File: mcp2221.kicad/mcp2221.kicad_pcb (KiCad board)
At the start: 2 copper layers, 71.5 x 45.4 mm, 24 parts, among them J1 Conn_01x07_Male, J2 Jumper 32 or 21, J3 Conn_01x02_Male, J4 Conn_01x02_Male, J5 Conn_01x04_Male, J6 Conn_01x03_Male, J7 Conn_01x03_Male, SW1 SW_Push, U1 AMS1117CD-3.3, U2 MCP2221

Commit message: pcb layout changes
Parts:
- moved SW1 36.7 mm to (111.8, 48.0), turned to 270 degrees
- moved R5 33.6 mm to (101.7, 49.1), turned to 270 degrees
- moved R8 32.0 mm to (74.0, 76.5), turned to 180 degrees
- moved J4 29.6 mm to (105.3, 49.9), turned to 0 degrees
- moved J3 23.9 mm to (87.2, 83.2)
- moved R1 22.3 mm to (106.8, 80.4), turned to 90 degrees
- moved R4 17.0 mm to (76.7, 82.7)
- moved J7 10.6 mm to (77.3, 77.3)
- moved J6 10.5 mm to (77.3, 73.5)
- moved R6 10.5 mm to (66.4, 73.7)
- moved R9 10.5 mm to (66.4, 82.7)
- moved D2 8.26 mm to (71.9, 79.8)
- moved D1 4.11 mm to (69.0, 79.6), turned to 180 degrees
- moved J1 1.68 mm to (91.4, 86.1)
- moved R7 1.61 mm to (74.0, 85.6), turned to 180 degrees
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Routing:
- added copper zone on B.Cu, net GND

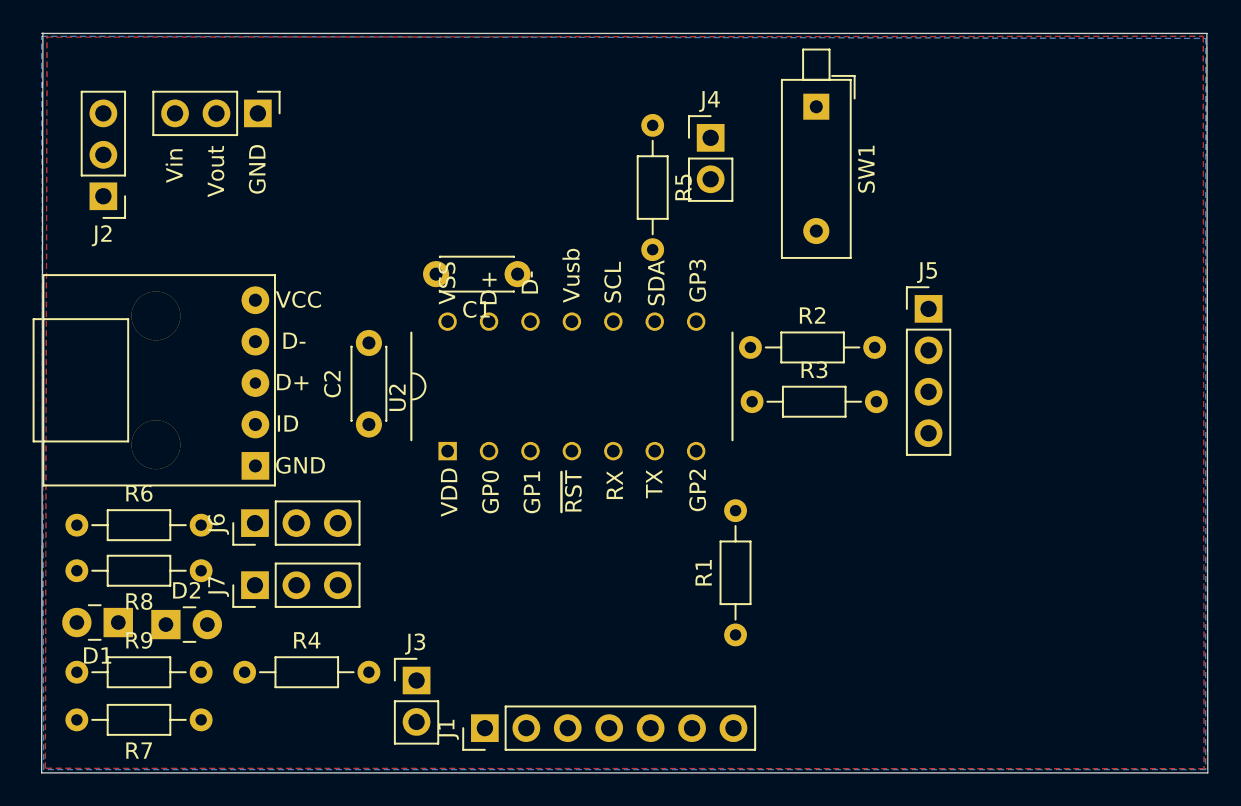
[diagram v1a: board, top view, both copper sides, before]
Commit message: initial layout for SMD
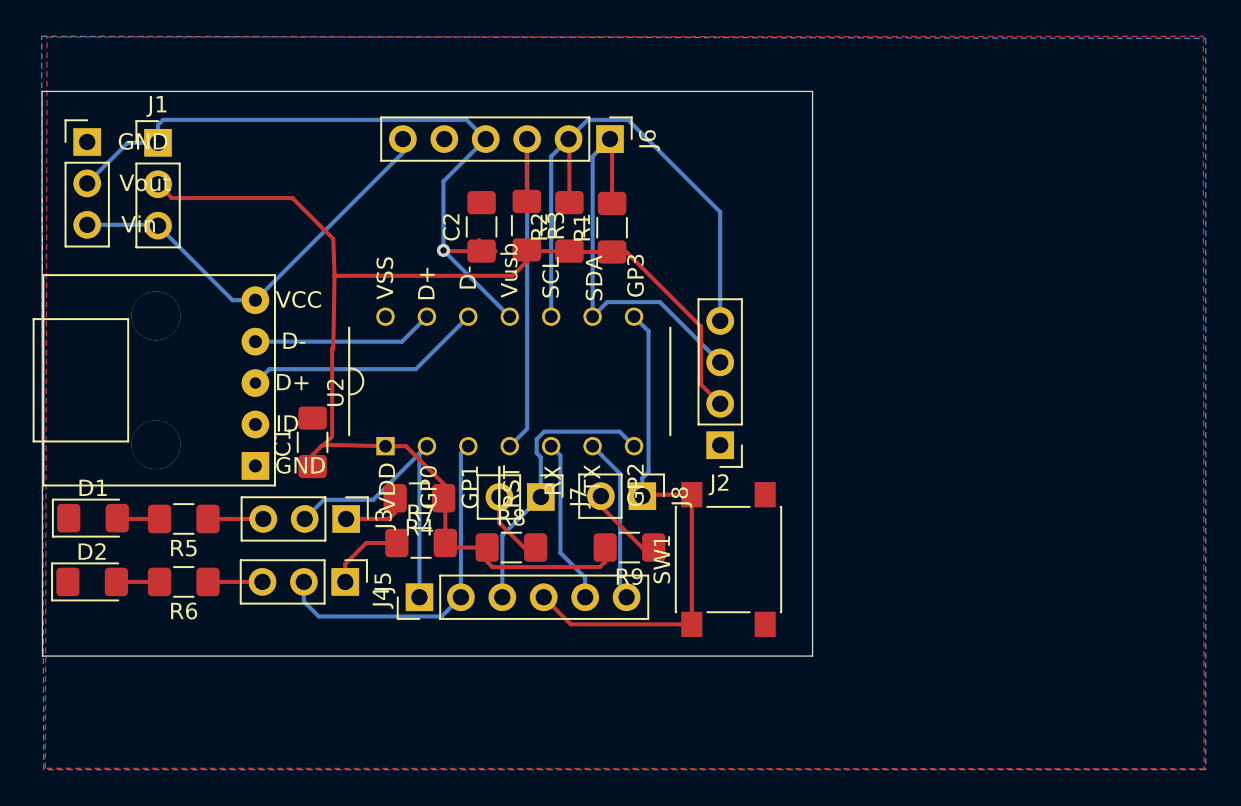
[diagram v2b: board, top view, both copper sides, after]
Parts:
- added J8: Conn_01x02_Male, Connector_PinHeader_2.54mm:PinHeader_1x02_P2.54mm_Vertical, F.Cu at (101.1, 71.9)
- C1: value 0.47µF -> 0.1 µF; footprint Capacitor_THT:C_Disc_D4.3mm_W1.9mm_P5.00mm -> Capacitor_SMD:C_1206_3216Metric_Pad1.42x1.75mm_HandSolder
- C2: value 0.1 µF -> 0.47µF; footprint Capacitor_THT:C_Disc_D4.3mm_W1.9mm_P5.00mm -> Capacitor_SMD:C_1206_3216Metric_Pad1.42x1.75mm_HandSolder
- D1, D2: footprint LED_THT:LED_Rectangular_W3.0mm_H2.0mm -> LED_SMD:LED_1206_3216Metric_Pad1.42x1.75mm_HandSolder
- J1: value Conn_01x07_Male -> Jumper 32 or 21; footprint Connector_PinHeader_2.54mm:PinHeader_1x07_P2.54mm_Vertical -> Connector_PinHeader_2.54mm:PinHeader_1x03_P2.54mm_Vertical
- J2: value Jumper 32 or 21 -> Conn_01x04_Male; footprint Connector_PinHeader_2.54mm:PinHeader_1x03_P2.54mm_Vertical -> Connector_PinHeader_2.54mm:PinHeader_1x04_P2.54mm_Vertical
- J3: value Conn_01x02_Male -> Conn_01x03_Male; footprint Connector_PinHeader_2.54mm:PinHeader_1x02_P2.54mm_Vertical -> Connector_PinHeader_2.54mm:PinHeader_1x03_P2.54mm_Vertical
- J4: value Conn_01x02_Male -> Conn_01x06_Male; footprint Connector_PinHeader_2.54mm:PinHeader_1x02_P2.54mm_Vertical -> Connector_PinHeader_2.54mm:PinHeader_1x06_P2.54mm_Vertical
- J5: value Conn_01x04_Male -> Conn_01x03_Male; footprint Connector_PinHeader_2.54mm:PinHeader_1x04_P2.54mm_Vertical -> Connector_PinHeader_2.54mm:PinHeader_1x03_P2.54mm_Vertical
- J6: value Conn_01x03_Male -> Conn_01x06_Male; footprint Connector_PinHeader_2.54mm:PinHeader_1x03_P2.54mm_Vertical -> Connector_PinHeader_2.54mm:PinHeader_1x06_P2.54mm_Vertical
- J7: value Conn_01x03_Male -> Conn_01x02_Male; footprint Connector_PinHeader_2.54mm:PinHeader_1x03_P2.54mm_Vertical -> Connector_PinHeader_2.54mm:PinHeader_1x02_P2.54mm_Vertical
- R1: value 10K -> 2.2k; footprint Resistor_THT:R_Axial_DIN0204_L3.6mm_D1.6mm_P7.62mm_Horizontal -> Resistor_SMD:R_1206_3216Metric_Pad1.42x1.75mm_HandSolder
- R2: value 2.2k -> 2.2K; footprint Resistor_THT:R_Axial_DIN0204_L3.6mm_D1.6mm_P7.62mm_Horizontal -> Resistor_SMD:R_1206_3216Metric_Pad1.42x1.75mm_HandSolder
- R3: value 2.2K -> 10K; footprint Resistor_THT:R_Axial_DIN0204_L3.6mm_D1.6mm_P7.62mm_Horizontal -> Resistor_SMD:R_1206_3216Metric_Pad1.42x1.75mm_HandSolder
- R4: value 2.2K -> 4.7K; footprint Resistor_THT:R_Axial_DIN0204_L3.6mm_D1.6mm_P7.62mm_Horizontal -> Resistor_SMD:R_1206_3216Metric_Pad1.42x1.75mm_HandSolder
- R5: value 2.2k -> 1K; footprint Resistor_THT:R_Axial_DIN0204_L3.6mm_D1.6mm_P7.62mm_Horizontal -> Resistor_SMD:R_1206_3216Metric_Pad1.42x1.75mm_HandSolder
- R6: value 2.2K -> 1K; footprint Resistor_THT:R_Axial_DIN0204_L3.6mm_D1.6mm_P7.62mm_Horizontal -> Resistor_SMD:R_1206_3216Metric_Pad1.42x1.75mm_HandSolder
- R7: value 2.2k -> 4.7K; footprint Resistor_THT:R_Axial_DIN0204_L3.6mm_D1.6mm_P7.62mm_Horizontal -> Resistor_SMD:R_1206_3216Metric_Pad1.42x1.75mm_HandSolder
- R8, R9: value 1K -> 4.7K; footprint Resistor_THT:R_Axial_DIN0204_L3.6mm_D1.6mm_P7.62mm_Horizontal -> Resistor_SMD:R_1206_3216Metric_Pad1.42x1.75mm_HandSolder
- SW1: footprint Button_Switch_THT:SW_DIP_SPSTx01_Piano_10.8x4.1mm_W7.62mm_P2.54mm -> Button_Switch_SMD:SW_Push_1P1T_NO_6x6mm_H9.5mm
- moved J1 41.1 mm to (71.4, 50.2), turned to 0 degrees
- moved J2 40.8 mm to (105.9, 68.8)
- moved J5 39.5 mm to (82.9, 77.1), turned to 270 degrees
- moved R5 37.5 mm to (73.0, 73.3), turned to 180 degrees
- moved R9 34.7 mm to (100.3, 75.0), turned to 180 degrees
- moved J4 33.4 mm to (87.4, 78.1), turned to 90 degrees
- moved J6 32.1 mm to (99.1, 50.0), turned to 270 degrees
- moved SW1 28.3 mm to (106.4, 75.8), turned to 90 degrees
- moved R1 26.1 mm to (99.2, 55.4)
- moved R8 19.1 mm to (93.1, 75.0), turned to 0 degrees
- moved J7 18.3 mm to (94.9, 71.9), turned to 270 degrees
- moved R3 17.5 mm to (94.0, 55.3), turned to 270 degrees
- moved R7 17.3 mm to (87.5, 74.8), turned to 0 degrees
- moved C1 16.3 mm to (80.9, 68.6), turned to 90 degrees
- moved R4 15.1 mm to (87.4, 72.0), turned to 180 degrees
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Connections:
- C1 pad 1: Net-(C1-Pad1) -> /VDD
- C2 pad 1: /VDD -> /3.3V
- J1 pad 1: /GP0 -> /3.3V
- J1 pad 2: /GP1 -> /VDD
- J1 pad 3: /GP2 -> /5V
- J2 pad 1: Net-(C1-Pad1) -> GND
- J2 pad 3: Net-(J2-Pad3) -> /SDA
- J3 pad 1: /GP2 -> Net-(J3-Pad1)
- J3 pad 2: Net-(J3-Pad2) -> /GP0
- J4 pad 1: Net-(J4-Pad1) -> /GP0
- J4 pad 2: /GP3 -> /GP1
- J5 pad 1: GND -> Net-(J5-Pad1)
- J5 pad 2: /VDD -> /GP1
- J5 pad 3: /SDA -> Net-(J5-Pad3)
- J6 pad 1: Net-(J6-Pad1) -> /SDA
- J6 pad 2: /GP0 -> /SCL
- J6 pad 3: Net-(J6-Pad3) -> /~RST~
- J7 pad 1: Net-(J7-Pad1) -> /GP2
- J7 pad 2: /GP1 -> Net-(J7-Pad2)
- R1 pad 1: /~RST~ -> /VDD
- R1 pad 2: /VDD -> /SDA
- R2 pad 2: /SDA -> /SCL
- R3 pad 1: /VDD -> /~RST~
- R3 pad 2: /SCL -> /VDD
- R4 pad 2: Net-(J3-Pad2) -> Net-(J3-Pad1)
- R5 pad 1: Net-(J4-Pad1) -> Net-(J3-Pad3)
- R5 pad 2: /VDD -> Net-(D1-Pad2)
- R6 pad 1: /VDD -> Net-(J5-Pad3)
- R6 pad 2: Net-(J6-Pad1) -> Net-(D2-Pad2)
- R7 pad 1: Net-(J7-Pad3) -> Net-(J5-Pad1)
- R8 pad 1: Net-(J6-Pad3) -> /VDD
- R8 pad 2: Net-(D1-Pad2) -> Net-(J7-Pad2)
- R9 pad 1: Net-(J7-Pad1) -> Net-(J8-Pad2)
- R9 pad 2: Net-(D2-Pad2) -> /VDD
- U1 pad 2: Net-(C1-Pad1) -> /3.3V
- U1 pad 3: Net-(J2-Pad3) -> /5V
- U2 pad 11: Net-(C1-Pad1) -> /3.3V
- USB1 pad 5: Net-(J2-Pad3) -> /5V
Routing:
- net /VDD: track 0.00 -> 81.3 mm
- net /3.3V: track 0.00 -> 44.8 mm, vias 0 -> 1
- net /SCL: track 0.00 -> 34.1 mm
- net /GP3: track 0.00 -> 32.3 mm
- net /5V: track 0.00 -> 25.9 mm
- net /SDA: track 0.00 -> 25.1 mm
- net /~RST~: track 0.00 -> 23.1 mm
- net /GP1: track 0.00 -> 21.1 mm
- net /GP0: track 0.00 -> 18.8 mm
- net /GP2: track 0.00 -> 17.3 mm
- net /USB-D-: track 0.00 -> 14.7 mm
- net /USB-D+: track 0.00 -> 11.2 mm
- net /TX: track 0.00 -> 10.1 mm
- net /RX: track 0.00 -> 10.1 mm
- net Net-(J8-Pad2): track 0.00 -> 4.91 mm
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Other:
- board size 71.5 x 45.4 mm -> 47.2 x 34.6 mm

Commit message: added text on F.Silks
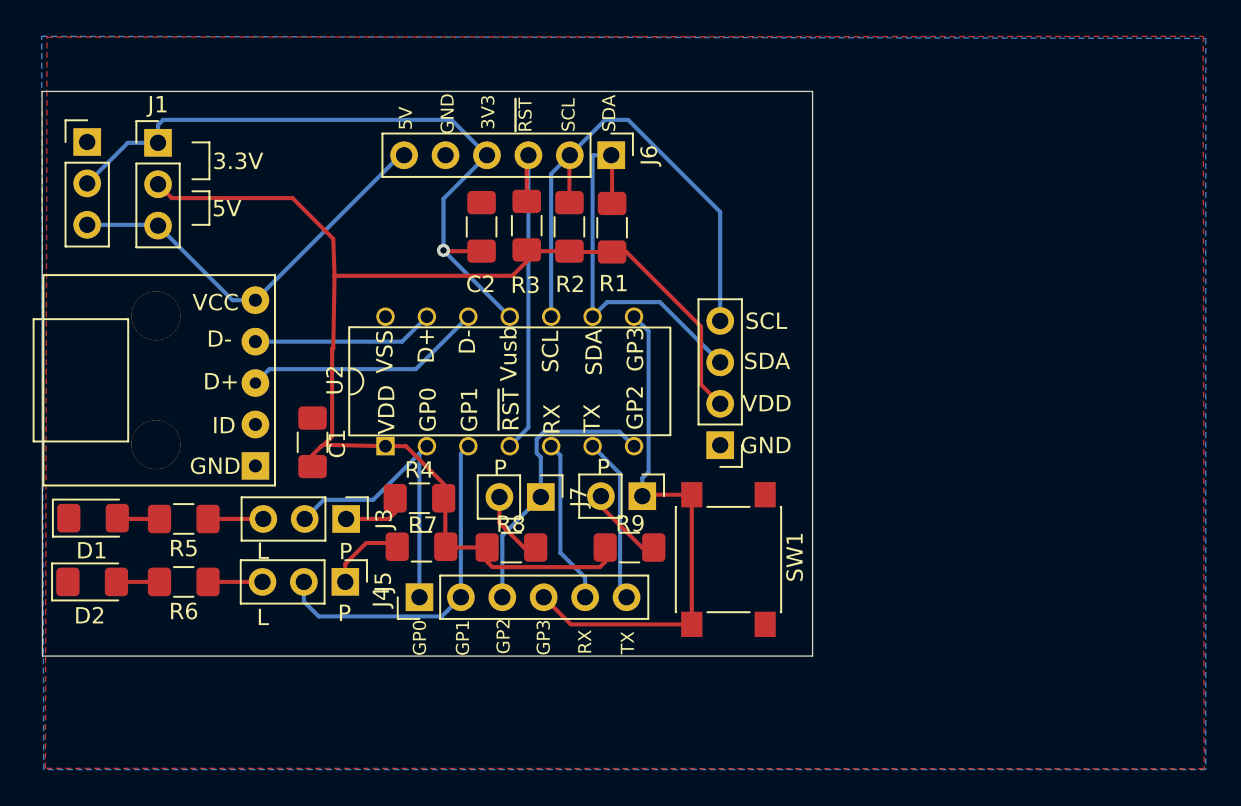
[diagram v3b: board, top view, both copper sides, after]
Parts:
- moved J6 0.99 mm to (99.2, 51.0)
- moved R7 0.23 mm to (87.6, 75.0)
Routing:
- net /3.3V: track 44.8 -> 42.7 mm
- net /~RST~: track 23.1 -> 21.2 mm
- net /SCL: track 34.1 -> 32.4 mm
- net /SDA: track 25.1 -> 23.7 mm
- net /5V: track 25.9 -> 25.0 mm
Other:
- board text added: "3.3V"
- board text added: "3V3"
- board text added: "5V"
- board text added: "GND"
- board text added: "GP0"
- board text added: "GP1"
- board text added: "GP2"
- board text added: "GP3"
- board text added: "L"
- board text added: "P"
- board text added: "RX"
- board text added: "SCL"
- board text added: "SDA"
- board text added: "TX"
- board text added: "VDD"
- board text added: "~RST~"

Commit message: updated footprint of AMS1117
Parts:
- moved J1 4.78 mm to (76.0, 49.1)
- moved U1 4.78 mm to (71.7, 49.0)
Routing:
- net /3.3V: track 42.7 -> 36.7 mm
- net /VDD: track 81.3 -> 77.1 mm
- net /5V: track 25.0 -> 23.3 mm

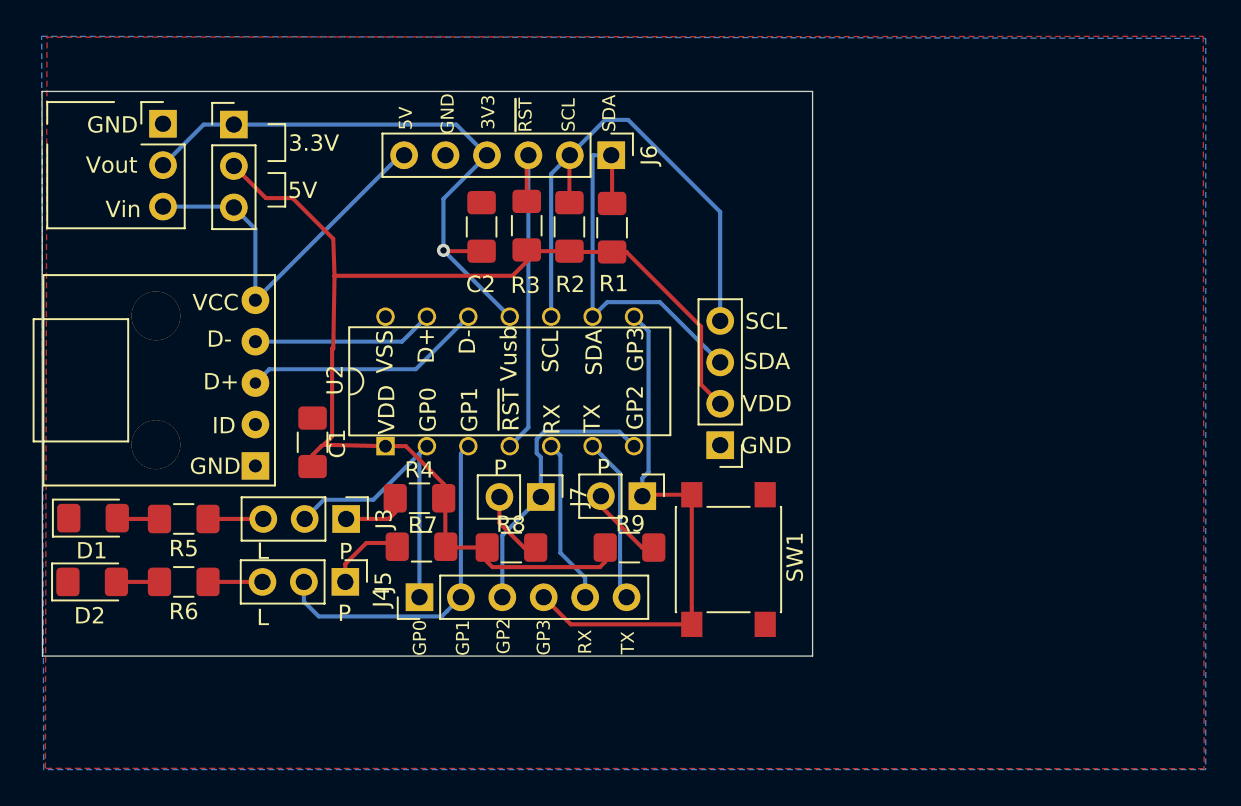
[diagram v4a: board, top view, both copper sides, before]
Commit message: changed track width of power-tracks
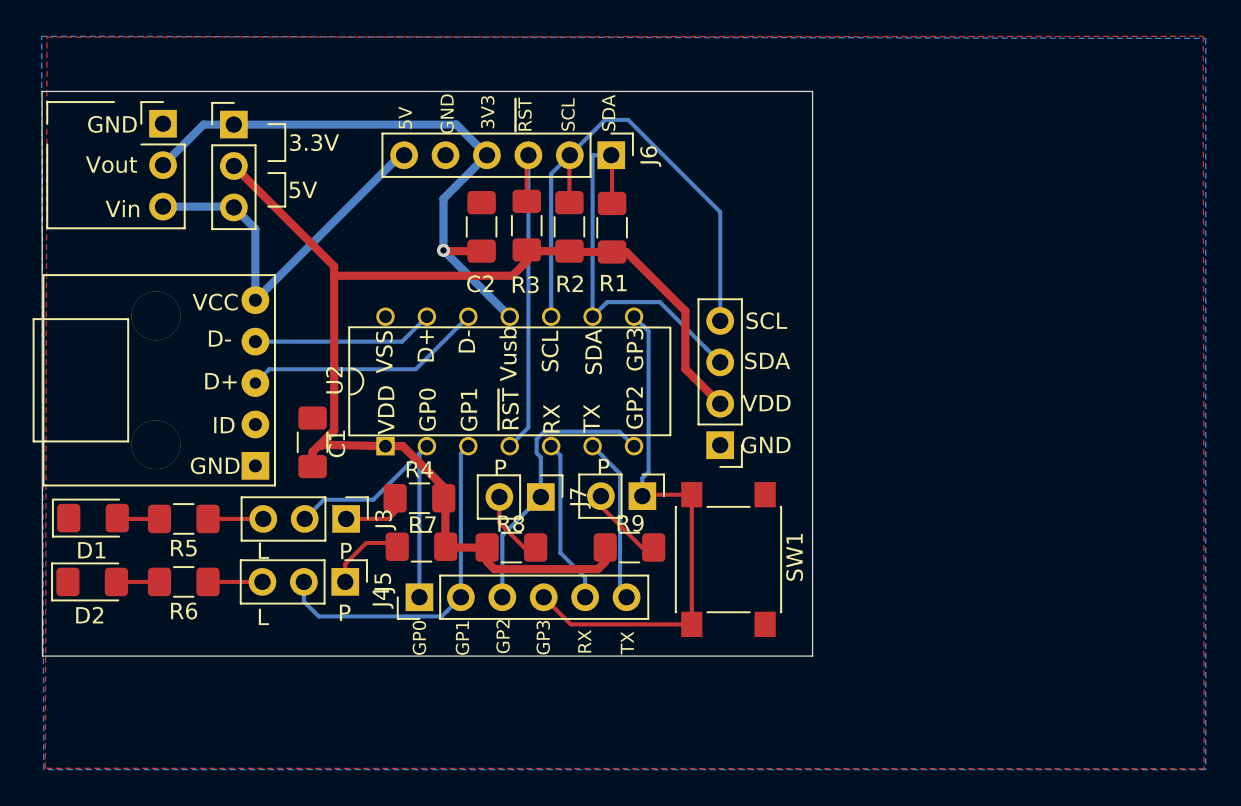
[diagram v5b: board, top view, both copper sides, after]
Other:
- net class 3V3 added: clearance 0.2, trace_width 0.5, via_dia 0.8, via_drill 0.4
- net class 5V added: clearance 0.2, trace_width 0.5, via_dia 0.8, via_drill 0.4
- net class VDD added: clearance 0.2, trace_width 0.5, via_dia 0.8, via_drill 0.4
